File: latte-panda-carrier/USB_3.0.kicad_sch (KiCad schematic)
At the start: 0 parts

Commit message: 160
Add USB
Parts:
- added C26, C27, C28, C29: 100nF/50V, A_HDJ_Library:C_0402_1005Metric, symbol Device:C_Small
- added C30, C31, C32: 22uF/50V, A_HDJ_Library:C_0603_1608Metric, symbol Device:C
- added D5, D7, D8, D9: ESD9B5.0ST5G, A_HDJ_Library:D_0402_1005Metric, symbol Diode:ESD9B5.0ST5G
- added F1, F2: 6V/1A, symbol Device:Fuse
- added F4, F5: 6V/2A, symbol Device:Fuse
- added J4: USB3_A_Stacked, A_HDJ_Library:USB3_A_Molex_48406-0001_Horizontal_Stacked, symbol Connector:USB3_A_Stacked
- added J5: USB_A_Stacked, A_HDJ_Library:USB_A_CUI_UJ2-ADH-TH_Horizontal_Stacked, symbol Connector:USB_A_Stacked
- added U3, U4, U5: D3V3XA4B10LP, A_HDJ_Library:Diodes_UDFN-10_1.0x2.5mm_P0.5mm, symbol Power_Protection:D3V3XA4B10LP
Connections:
- new net: F4.2, J4.1 (VBUS1)
- new net: F5.2, J4.10 (VBUS2)
- new net: F1.2, J5.1 (VBUS1)
- new net: F2.2, J5.5 (VBUS2)
- new net +5V: C30.2, C31.2, C32.2, F1.1, F2.1, F4.1, F5.1
- new net CON_USB3_SSTX_N: C26.2, J4.8 (SSTX1-)
- new net CON_USB3_SSTX_P: C27.2, J4.9 (SSTX1+)
- new net CON_USB4_SSTX_N: C28.2, J4.17 (SSTX2-)
- new net CON_USB4_SSTX_P: C29.2, J4.18 (SSTX2+)
- new net GND: C30.1, C31.1, C32.1, D5.1 (A1), D7.1 (A1), D8.1 (A1), D9.1 (A1), J4.13 (GND2), J4.16 (DRAIN2), J4.19 (SHIELD), J4.19 (SHIELD), J4.4 (GND1), J4.7 (DRAIN1), J5.4 (GND1), J5.8 (GND2), J5.9 (Shield), U3.3 (VSS), U3.8 (VSS), U4.3 (VSS), U4.8 (VSS), U5.3 (VSS), U5.8 (VSS)
- new net USB_2_P1-: J4.11 (D2-)
- new net USB_2_P2+: J4.12 (D2+)
- new net USB_2_P3+: D8.2 (A2), J5.7 (D2+), U4.4, U4.7 (NC)
- new net USB_2_P3-: D9.2 (A2), J5.6 (D2-), U4.5, U4.6 (NC)
- new net USB_2_P5+: D5.2 (A2), D7.2 (A2), J4.2 (D1-), J4.3 (D1+), J5.2 (D1-), J5.3 (D1+), U4.1, U4.10 (NC), U4.2, U4.9 (NC)
- new net USB_3_SSRX_N: J4.5 (SSRX1-), U3.2, U3.9 (NC)
- new net USB_3_SSRX_P: J4.6 (SSRX1+), U3.1, U3.10 (NC)
- new net USB_3_SSTX_N: C26.1, U5.2, U5.9 (NC)
- new net USB_3_SSTX_P: C27.1, U5.1, U5.10 (NC)
- new net USB_4_SSRT_N: C28.1, U5.5, U5.6 (NC)
- new net USB_4_SSRT_P: C29.1, U5.4, U5.7 (NC)
- new net USB_4_SSRX_N: J4.14 (SSRX2-), U3.5, U3.6 (NC)
- new net USB_4_SSRX_P: J4.15 (SSRX2+), U3.4, U3.7 (NC)
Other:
- note added: "USB 2.0 Data lines ESD protection"
- note added: "USB2"
- note added: "USB3/4"

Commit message: 160.2
Sheet pins for the USB. Also fix some labels.
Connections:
- net CON_USB3_SSTX_N: now also U5.1, U5.10 (NC)
- net CON_USB3_SSTX_P: now also U5.2, U5.9 (NC)
- net CON_USB4_SSTX_N: now also U5.4, U5.7 (NC)
- net CON_USB4_SSTX_P: now also U5.5, U5.6 (NC)
- net USB_2_P2+: now also J4.2 (D1-); no longer J4.12 (D2+)
- net USB_2_P5+: no longer D5.2 (A2), D7.2 (A2), J4.2 (D1-), J4.3 (D1+), J5.2 (D1-), U4.2, U4.9 (NC)
- net USB_3_SSRX_N: now also U3.1, U3.10 (NC); no longer U3.2, U3.9 (NC)
- net USB_3_SSRX_P: now also U3.2, U3.9 (NC); no longer U3.1, U3.10 (NC)
- net USB_3_SSTX_N: no longer U5.2, U5.9 (NC)
- net USB_3_SSTX_P: no longer U5.1, U5.10 (NC)
- net USB_4_SSRX_N: now also U3.4, U3.7 (NC); no longer U3.5, U3.6 (NC)
- net USB_4_SSRX_P: now also U3.5, U3.6 (NC); no longer U3.4, U3.7 (NC)
- removed net USB_4_SSRT_N: C28.1, U5.5, U5.6 (NC)
- removed net USB_4_SSRT_P: C29.1, U5.4, U5.7 (NC)
- new net USB_2_P1+: J4.12 (D2+)
- new net USB_2_P2-: D5.2 (A2), J4.3 (D1+)
- new net USB_2_P5-: D7.2 (A2), J5.2 (D1-), U4.2, U4.9 (NC)
- new net USB_4_SSTX_N: C28.1
- new net USB_4_SSTX_P: C29.1
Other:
- moved on the sheet: U3

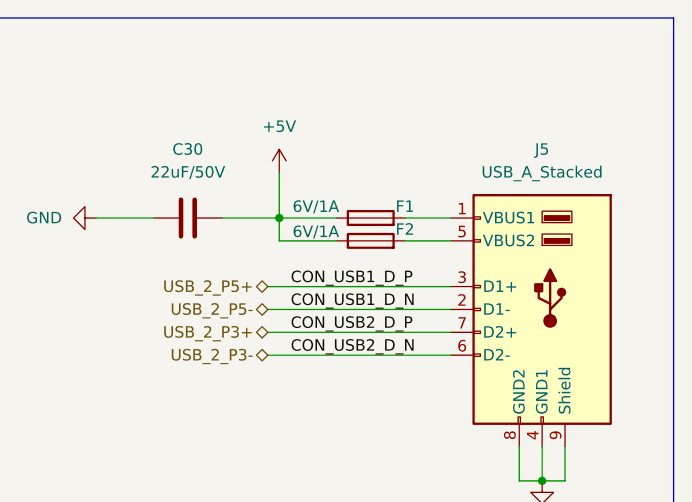
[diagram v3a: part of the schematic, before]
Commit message: Add m.2
Schematics stuff should be done, now.
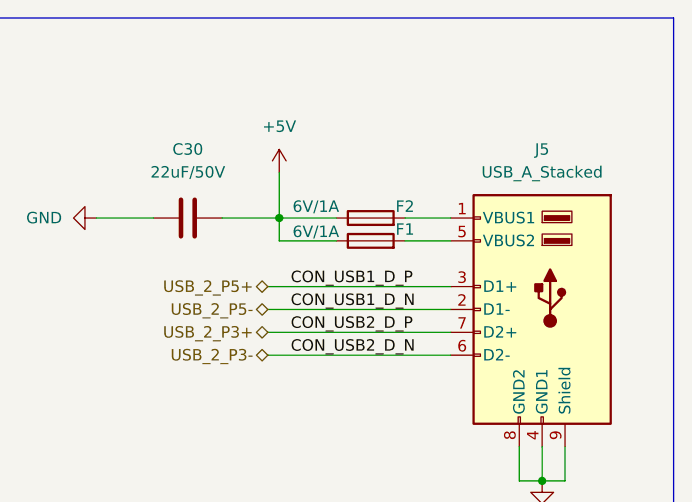
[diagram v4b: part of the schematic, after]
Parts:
- renumbered F2 to F1, F1 to F2
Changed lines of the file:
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@@
+		)
+	)
+	(label "CON_USB2_D_P"
+		(at 231.14 57.15 0)
+		(effects
+			(font
+				(size 1.27 1.27)
+			)
+			(justify left bottom)
+		)
+	)
+	(label "CON_USB4_SSRX_N"
+		(at 144.78 99.06 180)
+		(effects
+			(font
+				(size 1.27 1.27)
+			)
+			(justify right bottom)
+		)
+	)
+	(label "CON_USB4_SSTX_P"
+		(at 64.77 100.33 0)
+		(effects
+			(font
+				(size 1.27 1.27)
+			)
+			(justify left bottom)
+		)
+	)
+	(label "CON_USB3_SSRX_P"
+		(at 39.37 46.99 180)
+		(effects
+			(font
+				(size 1.27 1.27)
+			)
+			(justify right bottom)
+		)
+	)
+	(label "CON_USB2_D_N"
+		(at 231.14 59.69 0)
+		(effects
+			(font
+				(size 1.27 1.27)
+			)
+			(justify left bottom)
+		)
+	)
+	(label "CON_USB4_SSRX_P"
+		(at 64.77 46.99 0)
+		(effects
+			(font
+				(size 1.27 1.27)
+			)
+			(justify left bottom)
+		)
+	)
+	(label "CON_USB3_SSRX_N"
+		(at 144.78 46.99 180)
+		(effects
+			(font
+				(size 1.27 1.27)
+			)
+			(justify right bottom)
+		)
+	)
+	(label "CON_USB1_D_N"
+		(at 100.33 161.29 180)
+		(effects
+			(font
+				(size 1.27 1.27)
+			)
+			(justify right bottom)
+		)
+	)
+	(label "CON_USB1_D_N"
+		(at 231.14 54.61 0)
+		(effects
+			(font
+				(size 1.27 1.27)
+			)
+			(justify left bottom)
+		)
+	)
+	(label "CON_USB3_D_P"
+		(at 100.33 149.86 180)
+		(effects
+			(font
+				(size 1.27 1.27)
+			)
+			(justify right bottom)
+		)
+	)
+	(label "CON_USB4_SSRX_N"
+		(at 64.77 41.91 0)
+		(effects
+			(font
+				(size 1.27 1.27)
+			)
+			(justify left bottom)
+		)
+	)
+	(label "CON_USB3_SSRX_P"
+		(at 144.78 49.53 180)
+		(effects
+			(font
+				(size 1.27 1.27)
+			)
+			(justify right bottom)
+		)
+	)
+	(label "CON_USB4_SSRX_P"
+		(at 144.78 101.6 180)
+		(effects
+			(font
+				(size 1.27 1.27)
+			)
+			(justify right bottom)
 		)
 	)
@@
 		)
 	)
-	(label "CON_USB2_D_P"
-		(at 231.14 57.15 0)
-		(effects
-			(font
-				(size 1.27 1.27)
-			)
-			(justify left bottom)
-		)
-	)
-	(label "CON_USB2_D_N"
-		(at 231.14 59.69 0)
-		(effects
-			(font
-				(size 1.27 1.27)
-			)
-			(justify left bottom)
-		)
-	)
-	(label "CON_USB1_D_N"
-		(at 231.14 54.61 0)
-		(effects
-			(font
-				(size 1.27 1.27)
-			)
-			(justify left bottom)
-		)
-	)
-	(label "CON_USB4_SSRX_N"
-		(at 144.78 99.06 180)
-		(effects
-			(font
-				(size 1.27 1.27)
-			)
-			(justify right bottom)
-		)
-	)
-	(label "CON_USB4_SSTX_P"
-		(at 64.77 100.33 0)
-		(effects
-			(font
-				(size 1.27 1.27)
-			)
-			(justify left bottom)
-		)
-	)
-	(label "CON_USB3_SSRX_P"
-		(at 39.37 46.99 180)
-		(effects
-			(font
-				(size 1.27 1.27)
-			)
-			(justify right bottom)
-		)
-	)
-	(label "CON_USB4_SSRX_P"
-		(at 64.77 46.99 0)
-		(effects
-			(font
-				(size 1.27 1.27)
-			)
-			(justify left bottom)
-		)
-	)
-	(label "CON_USB3_SSRX_N"
-		(at 144.78 46.99 180)
-		(effects
-			(font
-				(size 1.27 1.27)
-			)
-			(justify right bottom)
-		)
-	)
-	(label "CON_USB1_D_N"
-		(at 100.33 161.29 180)
-		(effects
-			(font
-				(size 1.27 1.27)
-			)
-			(justify right bottom)
-		)
-	)
-	(label "CON_USB3_D_P"
-		(at 100.33 149.86 180)
-		(effects
-			(font
-				(size 1.27 1.27)
-			)
-			(justify right bottom)
-		)
-	)
-	(label "CON_USB4_SSRX_N"
-		(at 64.77 41.91 0)
-		(effects
-			(font
-				(size 1.27 1.27)
-			)
-			(justify left bottom)
-		)
-	)
-	(label "CON_USB3_SSRX_P"
-		(at 144.78 49.53 180)
-		(effects
-			(font
-				(size 1.27 1.27)
-			)
-			(justify right bottom)
-		)
-	)
-	(label "CON_USB4_SSRX_P"
-		(at 144.78 101.6 180)
-		(effects
-			(font
-				(size 1.27 1.27)
-			)
-			(justify right bottom)
-		)
-	)
 	(label "CON_USB3_SSTX_P"
 		(at 39.37 100.33 180)
@@
 			)
 			(justify right bottom)
+		)
+	)
+	(hierarchical_label "USB_2_P5-"
+		(shape bidirectional)
+		(at 228.6 54.61 180)
+		(effects
+			(font
+				(size 1.27 1.27)
+			)
+			(justify right)
+		)
+	)
+	(hierarchical_label "USB_2_P3-"
+		(shape bidirectional)
+		(at 228.6 59.69 180)
+		(effects
+			(font
+				(size 1.27 1.27)
+			)
+			(justify right)
 		)
 	)
@@
 		)
 	)
+	(hierarchical_label "USB_4_SSRX_N"
+		(shape input)
+		(at 104.14 99.06 180)
+		(effects
+			(font
+				(size 1.27 1.27)
+			)
+			(justify right)
+		)
+	)
 	(hierarchical_label "USB_3_SSTX_N"
 		(shape bidirectional)
@@
 		)
 	)
+	(hierarchical_label "USB_4_SSTX_P"
+		(shape output)
+		(at 104.14 109.22 180)
+		(effects
+			(font
+				(size 1.27 1.27)
+			)
+			(justify right)
+		)
+	)
 	(hierarchical_label "USB_3_SSRX_N"
 		(shape bidirectional)
@@
 		)
 	)
+	(hierarchical_label "USB_2_P3+"
+		(shape bidirectional)
+		(at 228.6 57.15 180)
+		(effects
+			(font
+				(size 1.27 1.27)
+			)
+			(justify right)
+		)
+	)
+	(hierarchical_label "USB_2_P1-"
+		(shape bidirectional)
+		(at 104.14 91.44 180)
+		(effects
+			(font
+				(size 1.27 1.27)
+			)
+			(justify right)
+		)
+	)
 	(hierarchical_label "USB_4_SSTX_N"
 		(shape output)
@@
 		)
 	)
-	(hierarchical_label "USB_4_SSRX_N"
-		(shape input)
-		(at 104.14 99.06 180)
+	(hierarchical_label "USB_3_SSTX_P"
+		(shape bidirectional)
+		(at 102.87 57.15 180)
+		(effects
+			(font
+				(size 1.27 1.27)
+			)
+			(justify right)
+		)
+	)
+	(hierarchical_label "USB_2_P1+"
+		(shape bidirectional)
+		(at 104.14 93.98 180)
+		(effects
+			(font
+				(size 1.27 1.27)
+			)
+			(justify right)
+		)
+	)
+	(hierarchical_label "USB_3_SSRX_P"
+		(shape bidirectional)
+		(at 102.87 49.53 180)
 		(effects
 			(font
@@
 		)
 	)
-	(hierarchical_label "USB_2_P1-"
-		(shape bidirectional)
-		(at 104.14 91.44 180)
-		(effects
-			(font
-				(size 1.27 1.27)
-			)
-			(justify right)
-		)
-	)
-	(hierarchical_label "USB_2_P1+"
-		(shape bidirectional)
-		(at 104.14 93.98 180)
-		(effects
-			(font
-				(size 1.27 1.27)
-			)
-			(justify right)
-		)
-	)
-	(hierarchical_label "USB_4_SSTX_P"
-		(shape output)
-		(at 104.14 109.22 180)
-		(effects
-			(font
-				(size 1.27 1.27)
-			)
-			(justify right)
-		)
-	)
-	(hierarchical_label "USB_3_SSTX_P"
-		(shape bidirectional)
-		(at 102.87 57.15 180)
-		(effects
-			(font
-				(size 1.27 1.27)
-			)
-			(justify right)
-		)
-	)
-	(hierarchical_label "USB_3_SSRX_P"
-		(shape bidirectional)
-		(at 102.87 49.53 180)
-		(effects
-			(font
-				(size 1.27 1.27)
-			)
-			(justify right)
-		)
-	)
 	(hierarchical_label "USB_2_P2+"
 		(shape bidirectional)
@@
 		)
 	)
-	(hierarchical_label "USB_2_P3+"
-		(shape bidirectional)
-		(at 228.6 57.15 180)
-		(effects
-			(font
-				(size 1.27 1.27)
-			)
-			(justify right)
-		)
-	)
-	(hierarchical_label "USB_2_P5-"
-		(shape bidirectional)
-		(at 228.6 54.61 180)
-		(effects
-			(font
-				(size 1.27 1.27)
-			)
-			(justify right)
-		)
-	)
 	(hierarchical_label "USB_2_P5+"
 		(shape bidirectional)
 		(at 228.6 52.07 180)
-		(effects
-			(font
-				(size 1.27 1.27)
-			)
-			(justify right)
-		)
-	)
-	(hierarchical_label "USB_2_P3-"
-		(shape bidirectional)
-		(at 228.6 59.69 180)
 		(effects
 			(font
@@
 		(on_board yes)
 		(dnp no)
-		(property "Reference" "F1"
+		(property "Reference" "F2"
 			(at 243.84 43.18 90)
 			(effects
@@
 			(project ""
 				(path "/9ba2df7d-1c0f-41ea-bb38-2c3f31e14521/3a6e79bf-a576-4fe6-99f9-6ed5ab5e0b5d"
-					(reference "F1")
+					(reference "F2")
 					(unit 1)
 				)
@@
 		(on_board yes)
 		(dnp no)
-		(property "Reference" "F2"
+		(property "Reference" "F1"
 			(at 243.84 45.72 90)
 			(effects
@@
 			(project "latte-panda-carrier"
 				(path "/9ba2df7d-1c0f-41ea-bb38-2c3f31e14521/3a6e79bf-a576-4fe6-99f9-6ed5ab5e0b5d"
-					(reference "F2")
-					(unit 1)
-				)
+					(reference "F1")
+					(unit 1)
+				)
